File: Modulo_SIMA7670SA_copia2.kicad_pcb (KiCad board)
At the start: 2 copper layers, 90.3 x 85 mm, 57 parts, among them J1 TBP01R1-508-02BE, J2 DB9 Hembra Impreso 90°, J3 U.FL IPEX1 MALE, J4 SMA-J-P-X-RA-TH1, J5 Jack DC 2.1mm PCB recto, Q1 BSS138, Q2 FDN340P, Q3 FDN340P, Q4 BSS138, U1 MAX232, U2 24LC512, U3 BKP-A7670SA (Módulo SIMCOM), U5 Black_Pill_STM32F411CEUx, U6 LM2596S_Modulo_Regulable, U7 LM7805_TO220

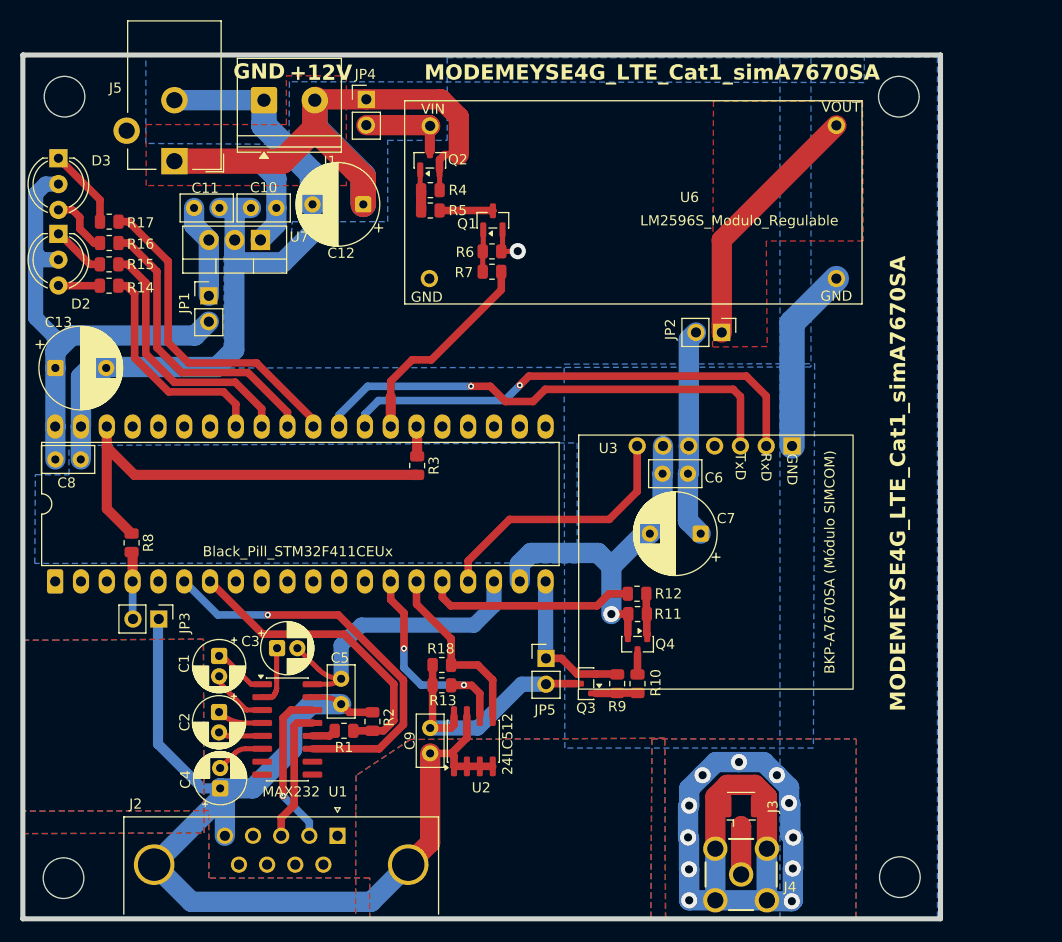
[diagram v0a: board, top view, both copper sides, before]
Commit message: fix(pcb): consolidar zonas de cobre y priorizar plano de GND
- Resolver nombre de zona duplicado ("Pour7" x2 -> renombrado a
  "Pour10")
- Restaurar "RF_LTE_4G" como prioridad maxima del board (10)
- Agregar zona adicional de GND (Pour11) para reforzar cobertura
  de plano
- Reordenar prioridades: +12V y Net-(JP2-A) por debajo del plano
  de GND en las zonas donde corresponde

Nota de diseno: colisiones de courtyard entre U3/U6/U5 y componentes
chicos (R3-R12, Q1-Q4, C6-C9) son intencionales y no criticas -
estos IC montan sobre zocalo con elevacion suficiente para alojar
partes debajo. Excluir estas violaciones puntuales en el DRC de
KiCad (Exclude this violation) para mantener el resto de las
verificaciones limpias.

Pendiente para el proximo commit: la zona "A", ubicada sobre J3
(conector de antena U.FL), figura todavia con net +12V en el
archivo actual - debe pasar a GND (confirmado con Damian, cambio
realizado localmente pero no reflejado aun en el archivo
compartido). Verificar clearance contra los pads de GND de J3
una vez actualizado.
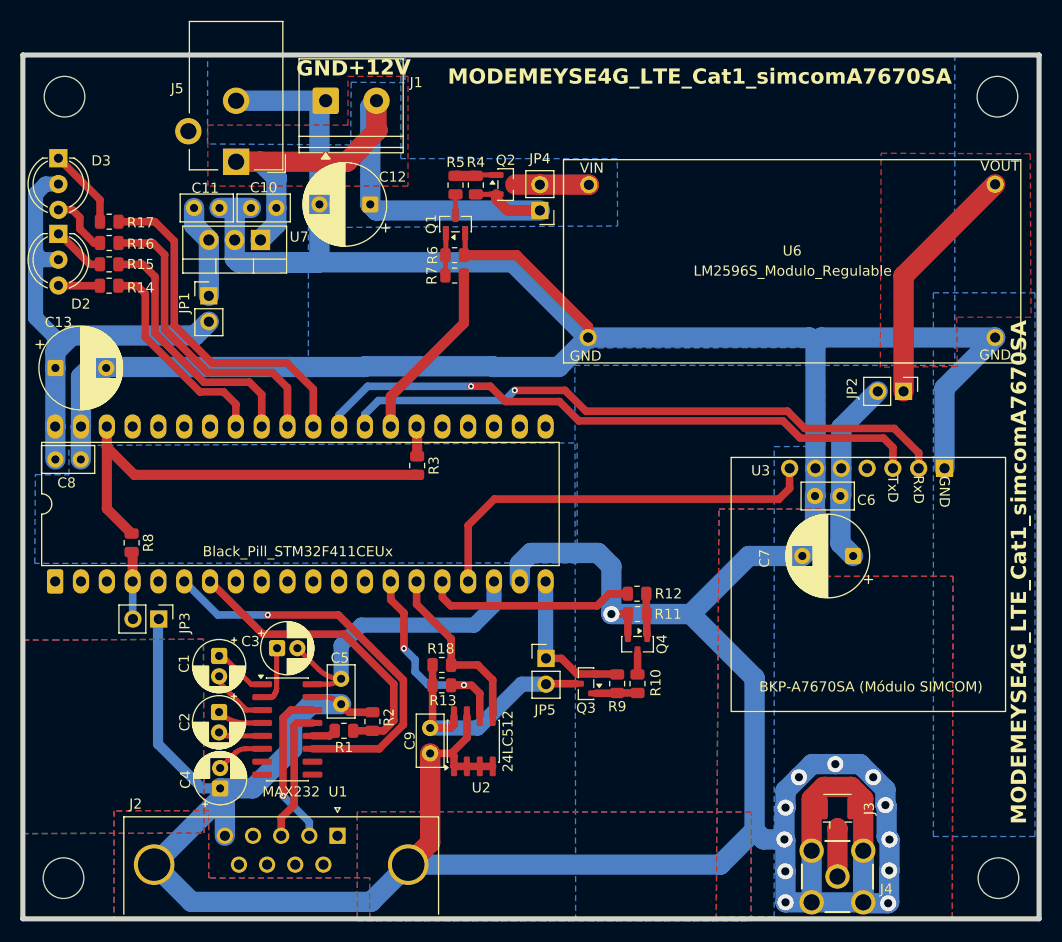
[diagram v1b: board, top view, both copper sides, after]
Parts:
- moved JP4 20.3 mm to (165.7, 76.0), turned to 180 degrees
- moved JP2 18.8 mm to (201.5, 93.8)
- moved U6 16.7 mm to (190.6, 81.0)
- moved C6 15.2 mm to (195.3, 104.1)
- moved U3 15.2 mm to (198.1, 112.8)
- moved C7 15.2 mm to (196.6, 110.0)
- moved H4 9.70 mm to (210.9, 141.7)
- moved H3 9.70 mm to (210.8, 64.8)
- moved J3 9.48 mm to (195.0, 135.3)
- moved J4 9.48 mm to (195.0, 141.5)
- moved Q2 7.84 mm to (162.4, 73.4), turned to 0 degrees
- moved J1 6.07 mm to (144.7, 65.2)
- moved J5 6.07 mm to (135.8, 71.2)
- moved R4 4.50 mm to (159.4, 73.5), turned to 90 degrees
- moved Q1 3.69 mm to (157.4, 77.3)
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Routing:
- net GND: track 316.4 -> 520.4 mm, vias 13 -> 12
- net +12V: track 80.6 -> 64.3 mm
- net SLEEP_MODEM: track 26.0 -> 40.6 mm
- net UART2_RX: track 48.1 -> 61.4 mm
- net UART2_TX: track 48.0 -> 60.7 mm
- net Net-(Q1-D): track 5.25 -> 1.99 mm
- net ON_MODEM: track 20.9 -> 17.8 mm
- net 5V_MODEM: track 20.6 -> 18.2 mm
- net Net-(U5-PA4): track 32.6 -> 34.5 mm
- net 12V_StepDown: track 8.77 -> 7.26 mm
- net Net-(U5-PA5): track 29.3 -> 30.6 mm
- net Net-(U5-PA7): track 22.3 -> 21.1 mm
- net Net-(JP2-A): track 25.0 -> 24.1 mm
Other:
- board size 90.3 x 85 mm -> 100 x 85 mm
- board text added: "MODEMEYSE4G_LTE_Cat1_simcomA7670SA"
- board text removed: "MODEMEYSE4G_LTE_Cat1_simA7670SA"
